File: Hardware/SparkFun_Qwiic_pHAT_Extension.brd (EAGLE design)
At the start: 65 x 78.4 mm, 77 parts, among them J1 RASPBERRYPI-40-PIN-GPIO_SMD_M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, J2 RASPBERRYPI-40-PIN-GPIO_RIGHT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, J3 QWIIC_RIGHT_ANGLE, J5 QWIIC_RIGHT_ANGLE

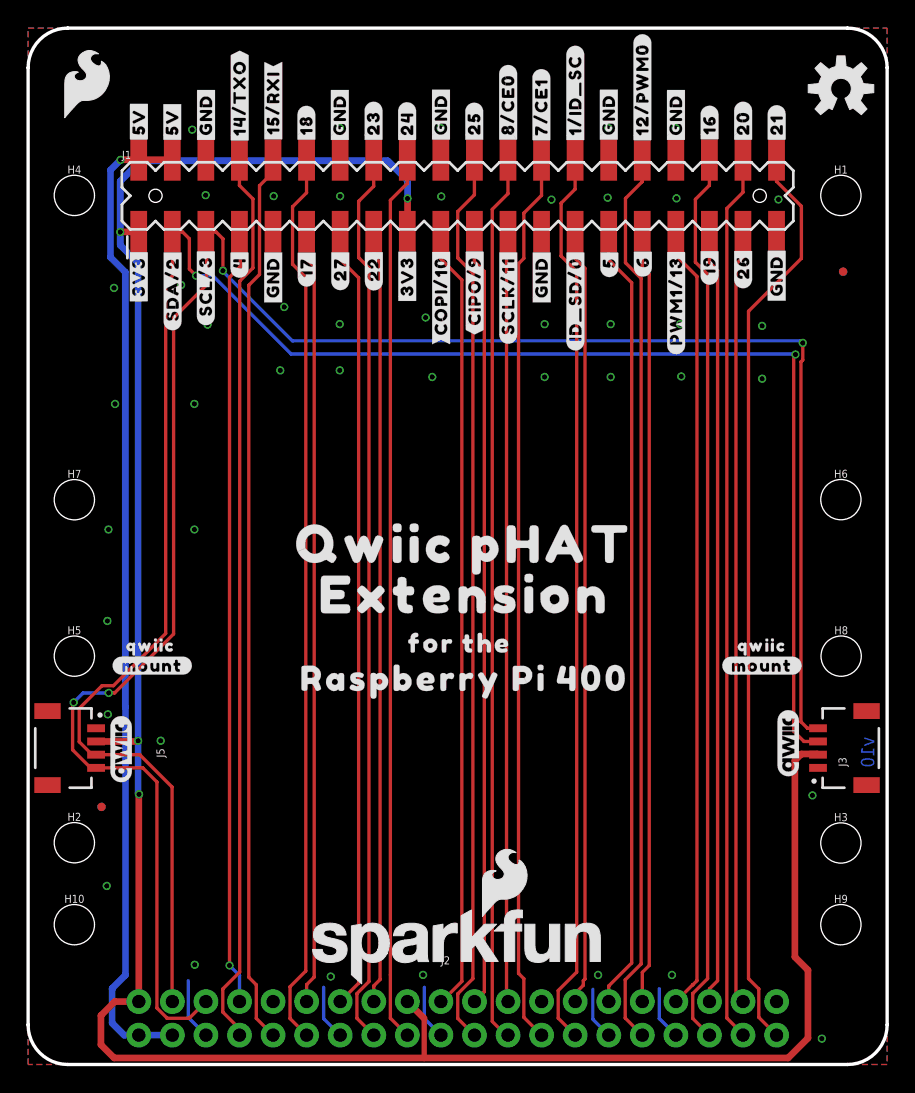
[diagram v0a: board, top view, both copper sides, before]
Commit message: Fixes PWM net names, fixes measures to account for moved stand offs
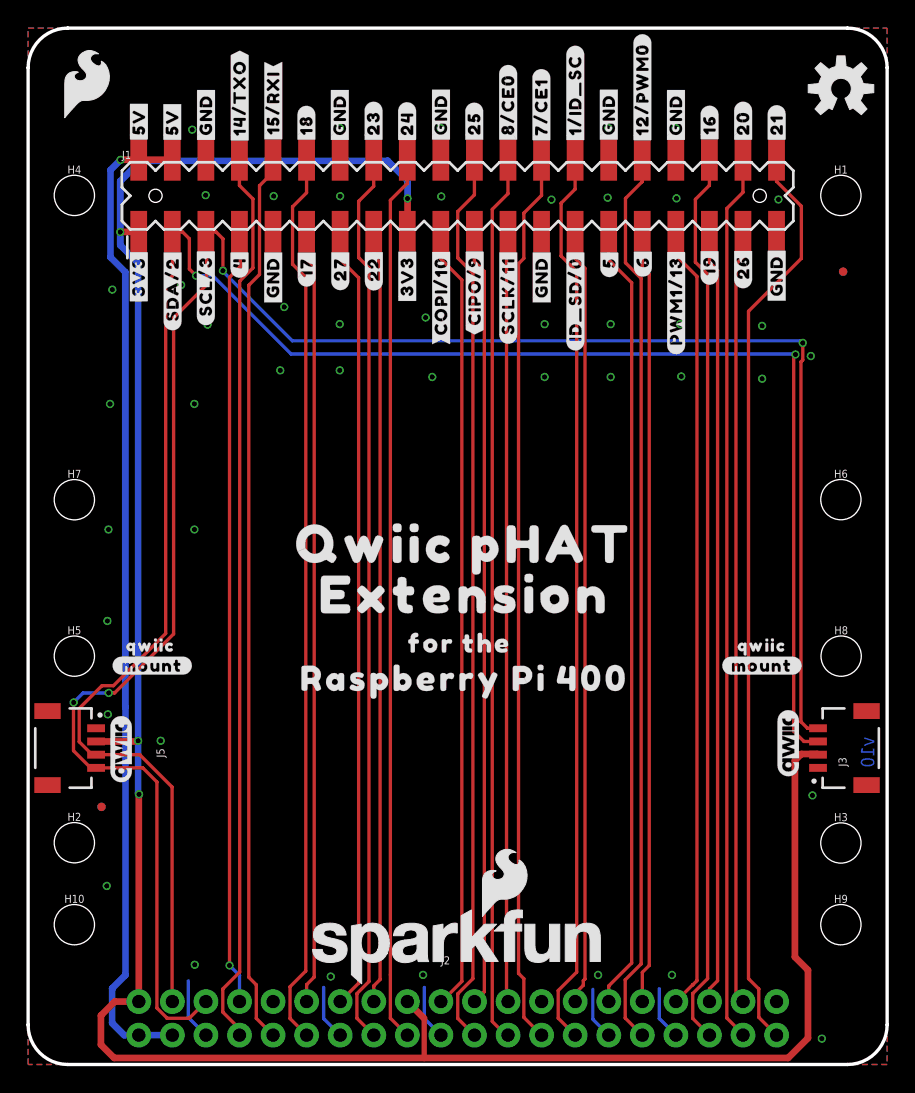
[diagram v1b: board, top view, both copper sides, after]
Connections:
- net 12/PCM0 renamed 12/PWM0
- net 13/PCM1 renamed 13/PWM1
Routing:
- net GND: vias 45 -> 46
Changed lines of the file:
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@@
 <setting verticaltext="up"/>
 </settings>
-<grid distance="0.5" unitdist="mm" unit="mm" style="dots" multiple="1" display="yes" altdistance="0.01" altunitdist="mm" altunit="mm"/>
+<grid distance="0.05" unitdist="inch" unit="inch" style="dots" multiple="1" display="yes" altdistance="0.005" altunitdist="inch" altunit="inch"/>
 <layers>
 <layer number="1" name="Top" color="4" fill="1" visible="yes" active="yes"/>
@@
 <layer number="37" name="tTest" color="7" fill="1" visible="no" active="yes"/>
 <layer number="38" name="bTest" color="7" fill="1" visible="no" active="yes"/>
-<layer number="39" name="tKeepout" color="4" fill="11" visible="yes" active="yes"/>
+<layer number="39" name="tKeepout" color="4" fill="11" visible="no" active="yes"/>
 <layer number="40" name="bKeepout" color="1" fill="11" visible="no" active="yes"/>
 <layer number="41" name="tRestrict" color="4" fill="10" visible="no" active="yes"/>
@@
 <layer number="49" name="Reference" color="13" fill="1" visible="yes" active="yes"/>
 <layer number="50" name="dxf" color="7" fill="1" visible="no" active="yes"/>
-<layer number="51" name="tDocu" color="6" fill="1" visible="no" active="yes"/>
+<layer number="51" name="tDocu" color="6" fill="1" visible="yes" active="yes"/>
 <layer number="52" name="bDocu" color="7" fill="1" visible="no" active="yes"/>
 <layer number="53" name="tGND_GNDA" color="7" fill="9" visible="no" active="no"/>
@@
 <dimension x1="2.99" y1="13.266" x2="2.99" y2="0.006" x3="-8" y3="6.636" textsize="1.778" textratio="15" layer="47" visible="yes"/>
 <dimension x1="-0.01" y1="0.006" x2="0" y2="16.73" x3="-11.505290625" y3="8.374875" textsize="1.778" textratio="15" layer="47" visible="yes"/>
-<dimension x1="-0.01" y1="0.006" x2="0" y2="26.94" x3="-15.0057375" y3="13.47856875" textsize="1.778" textratio="15" layer="47" visible="yes"/>
-<dimension x1="-0.01" y1="0.006" x2="0" y2="37" x3="-19.005675" y3="18.508134375" textsize="1.778" textratio="15" layer="47" visible="yes"/>
+<dimension x1="-0.01" y1="0.006" x2="0" y2="24.019" x3="-15.0057375" y3="12.018746875" textsize="1.778" textratio="15" layer="47" visible="yes"/>
+<dimension x1="-0.01" y1="0.006" x2="0" y2="30.904" x3="-19.005675" y3="15.46115" textsize="1.778" textratio="15" layer="47" visible="yes"/>
 <dimension x1="-0.01" y1="0.006" x2="0" y2="42.7" x3="-23.005465625" y3="21.358384375" textsize="1.778" textratio="15" layer="47" visible="yes"/>
 <dimension x1="3.49" y1="65.766" x2="3.5" y2="78.5" x3="-8.0053875" y3="72.14203125" textsize="1.778" textratio="15" layer="47" visible="yes"/>
 <dimension x1="-0.01" y1="0.006" x2="-0.01" y2="78.425" x3="-29" y3="39.2155" textsize="1.778" textratio="15" layer="47" visible="yes"/>
-<dimension x1="61.49" y1="37.084" x2="61.49" y2="42.746" x3="72" y3="39.915" textsize="1.778" textratio="15" layer="47" visible="yes"/>
 <text x="64.02" y="24.81" size="1.016" layer="16" font="vector" ratio="15" rot="SMR270">v10</text>
+<dimension x1="61.49" y1="10.584" x2="61.468" y2="-0.127" x3="76.210678125" y3="5.198240625" textsize="1.778" textratio="15" layer="47" visible="yes"/>
 </plain>
 <attributes>
@@
 <wire x1="14.732" y1="60.071" x2="14.732" y2="62.484" width="0.254" layer="1"/>
 <via x="58.607" y="54.604" extent="1-16" drill="0.381"/>
-<wire x1="3.357" y1="23.813" x2="3.357" y2="27.32" width="0.254" layer="1"/>
-<wire x1="3.357" y1="27.32" x2="3.437" y2="27.4" width="0.254" layer="1"/>
 <via x="3.437" y="27.4" extent="1-16" drill="0.381"/>
 <via x="6.087" y="28.1199" extent="1-16" drill="0.381"/>
@@
 <wire x1="6.537" y1="28.1199" x2="6.087" y2="28.1199" width="0.254" layer="1"/>
 <wire x1="4.1569" y1="28.1199" x2="6.087" y2="28.1199" width="0.254" layer="16"/>
-<wire x1="3.437003125" y1="27.400003125" x2="4.1569" y2="28.1199" width="0.254" layer="16"/>
 <wire x1="4.722" y1="22.448" x2="5.1326" y2="22.448" width="0.254" layer="1"/>
-<wire x1="3.357" y1="23.813" x2="4.722" y2="22.448" width="0.254" layer="1"/>
+<wire x1="3.425" y1="23.745" x2="4.722" y2="22.448" width="0.254" layer="1"/>
 <wire x1="9.737" y1="21.38" x2="8.669" y2="22.448" width="0.254" layer="1"/>
 <wire x1="8.669" y1="22.448" x2="5.1326" y2="22.448" width="0.254" layer="1"/>
-<wire x1="3.437" y1="27.4" x2="3.437003125" y2="27.400003125" width="0" layer="19" extent="16-16"/>
+<wire x1="3.425" y1="23.745" x2="3.425" y2="27.388" width="0.254" layer="1"/>
+<wire x1="3.425" y1="27.388" x2="3.437" y2="27.4" width="0.254" layer="1"/>
+<wire x1="3.437" y1="27.4" x2="4.1569" y2="28.1199" width="0.254" layer="16"/>
 </signal>
 <signal name="GND">
@@
 <vertex x="64.99" y="0.006"/>
 </polygon>
-<via x="6.49" y="58.766" extent="1-16" drill="0.381"/>
+<via x="6.363" y="58.639" extent="1-16" drill="0.381"/>
 <via x="13.57" y="55.986" extent="1-16" drill="0.381"/>
 <via x="23.57" y="56.026" extent="1-16" drill="0.381"/>
@@
 <via x="5.94" y="13.516" extent="1-16" drill="0.381"/>
 <via x="6.07" y="40.486" extent="1-16" drill="0.381"/>
-<via x="6.57" y="49.986" extent="1-16" drill="0.381"/>
+<via x="6.189" y="49.986" extent="1-16" drill="0.381"/>
 <via x="12.57" y="49.986" extent="1-16" drill="0.381"/>
 <via x="12.57" y="40.486" extent="1-16" drill="0.381"/>
@@
 <via x="29.874" y="6.787" extent="1-16" drill="0.381"/>
 <via x="6.0238" y="26.5018" extent="1-16" drill="0.381"/>
+<via x="59.213" y="53.61" extent="1-16" drill="0.381"/>
 </signal>
 <signal name="GP4">
@@
 <wire x1="35.11" y1="3.2614" x2="35.11" y2="64.71" width="0.254" layer="1"/>
 </signal>
-<signal name="12/PCM0">
+<signal name="12/PWM0">
 <contactref element="J1" pad="32"/>
 <contactref element="J2" pad="32"/>
@@
 <wire x1="45.17" y1="6.41" x2="46.3754" y2="7.6154" width="0.254" layer="1"/>
 </signal>
-<signal name="13/PCM1">
+<signal name="13/PWM1">
 <contactref element="J1" pad="33"/>
 <contactref element="J2" pad="33"/>
